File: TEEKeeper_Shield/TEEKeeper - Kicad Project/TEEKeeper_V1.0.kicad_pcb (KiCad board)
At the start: 2 copper layers, 99.4 x 94.5 mm, 29 parts

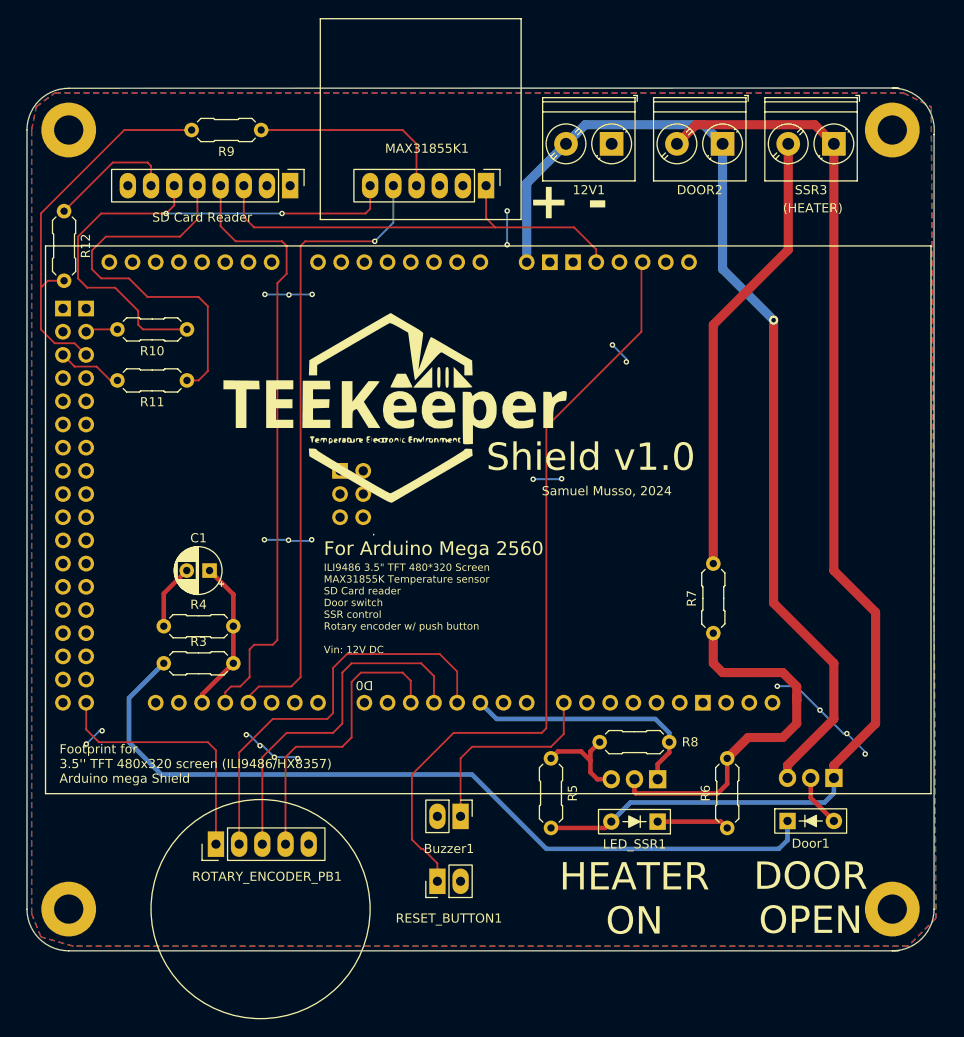
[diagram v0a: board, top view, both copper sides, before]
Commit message: Resolved minor issues
Fixed broken / bad designed reference connections, fixed pcb courtyard and edges, general cleanup
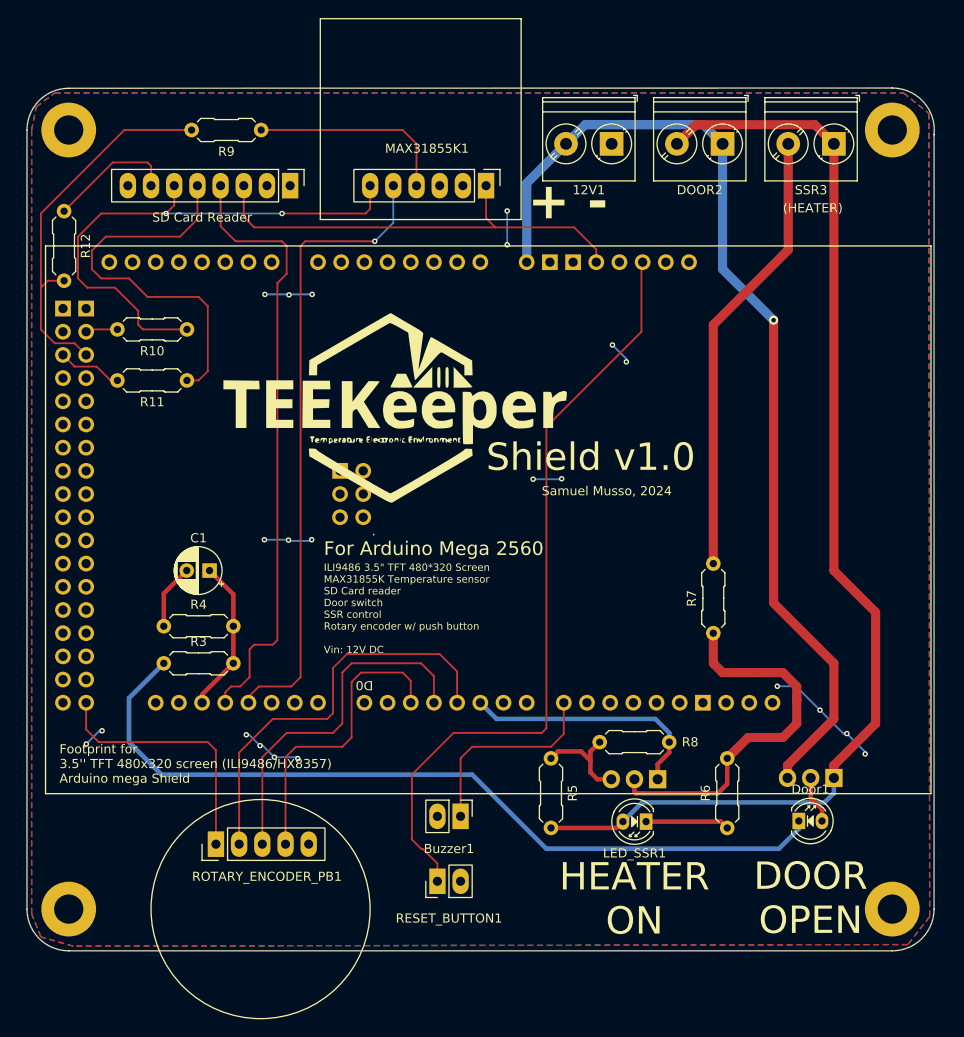
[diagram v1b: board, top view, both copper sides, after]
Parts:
- Door1, LED_SSR1: footprint PCM_LED_THT_AKL:LED_Indicator_D1.8mm_W2.44mm_L7.62mm -> PCM_LED_THT_AKL:LED_D4.0mm
- moved LED_SSR1 1.27 mm to (192.3, 106.2)
- moved Door1 1.24 mm to (209.0, 106.2)
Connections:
- A1 pad 5V1: /System_Shield/Digital_PCB/5V -> 5V
- A1 pad 5V3: /System_Shield/Digital_PCB/5V -> 5V
- A1 pad 5V4: /System_Shield/Digital_PCB/5V -> unconnected-(A1-5V-Pad5V4)
- MAX31855K1 pad 1: /System_Shield/Digital_PCB/5V -> 5V
- ROTARY_ENCODER_PB1 pad 1: /System_Shield/Digital_PCB/5V -> 5V
- SD_CARD1 pad 3: /System_Shield/Digital_PCB/5V -> 5V
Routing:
- net 5V: track 0.00 -> 78.3 mm
- net /System_Shield/Digital_PCB/5V: track 78.3 -> 0.00 mm
- net Net-(LED_SSR1-Pad1): track 7.91 -> 9.17 mm
- net Net-(P_DOOR1-D): track 5.77 -> 5.23 mm
- net Net-(Door1-Pad1): track 89.7 -> 90.2 mm
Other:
- outline, holes or cut-outs redrawn

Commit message: Minor changes
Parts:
- moved ROTARY_ENCODER_PB1 3.43 mm to (141.7, 108.7)
- moved R6 2.54 mm to (198.6, 106.9)
- moved R8 2.54 mm to (184.7, 97.5)
- moved RESET_BUTTON1 2.54 mm to (166.9, 112.8)
- moved Buzzer1 2.54 mm to (169.4, 105.7)
- moved Door1 2.54 mm to (206.5, 106.2)
- moved LED_SSR1 2.54 mm to (189.7, 106.2)
- moved N_SSR1 2.54 mm to (191.0, 101.6)
- moved P_DOOR1 2.54 mm to (210.3, 101.5)
- moved R5 2.54 mm to (179.3, 99.3)
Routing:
- net GND: track 60.2 -> 84.0 mm, vias 22 -> 30
- net 5V: track 78.3 -> 74.8 mm
- net /System_Shield/Digital_PCB/D4: track 45.5 -> 48.7 mm
- net /System_Shield/Digital_PCB/D2_INTRR: track 33.4 -> 36.6 mm
- net /System_Shield/Digital_PCB/D3_INTRR: track 39.4 -> 42.6 mm
- net /System_Shield/Analog_PCB/HEATER_CT: track 27.7 -> 25.1 mm
- net Net-(N_SSR1-D): track 42.1 -> 44.1 mm
- net Net-(P_DOOR1-G): track 126.4 -> 124.9 mm
- net Net-(Door1-Pad1): track 90.2 -> 88.7 mm
- net /System_Shield/Digital_PCB/RESET: track 85.2 -> 84.3 mm
- net /System_Shield/Digital_PCB/BUZ: track 22.2 -> 22.7 mm

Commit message: Added connector cutouts
Added cutouts for the Arduino Mega barrel and USB-A connector. 
Rerouted connections accordingly.
Added more vias to GND plane along SPI lines and other parallel strips. 
Added clearance for some components.
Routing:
- net /System_Shield/Digital_PCB/D4: track 48.7 -> 52.8 mm
- net GND: track 84.0 -> 86.3 mm, vias 30 -> 123
- net Net-(P_DOOR1-G): track 124.9 -> 127.0 mm
- net /System_Shield/Digital_PCB/D3_INTRR: track 42.6 -> 44.5 mm
- net Net-(Door1-Pad1): track 88.7 -> 87.7 mm
- net Net-(N_SSR1-D): track 44.1 -> 43.6 mm
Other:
- outline, holes or cut-outs redrawn

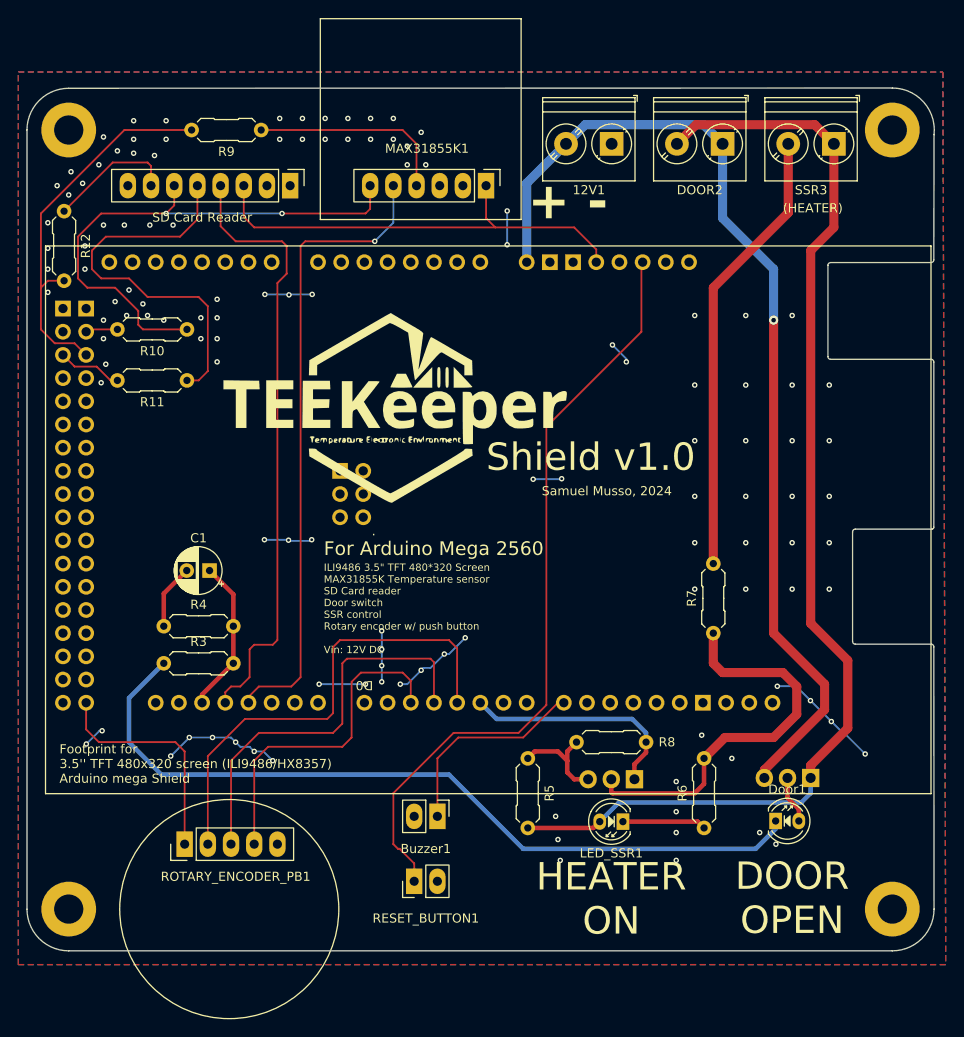
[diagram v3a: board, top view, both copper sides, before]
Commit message: Reworked Arduino Mega clearance
Due to some clones having their USB and barrel connector placed in slightly different locations, added a big cutout and rerouted tracks accordingly

uniformed 12V copper lines width
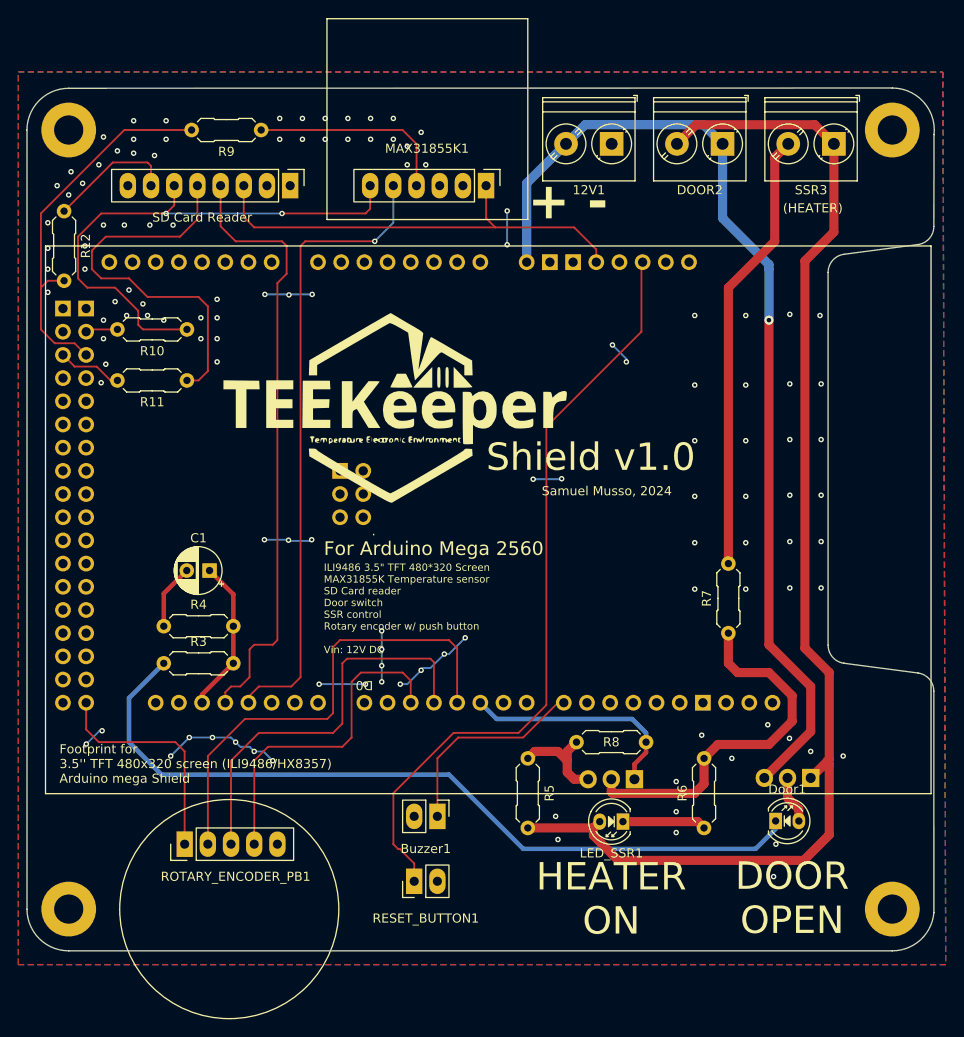
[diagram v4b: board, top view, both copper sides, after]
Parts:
- moved R7 1.65 mm to (201.3, 85.6)
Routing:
- net GND: track 86.3 -> 73.6 mm, vias 123 -> 122
- net Net-(P_DOOR1-G): track 127.0 -> 136.9 mm
- net Net-(N_SSR1-D): track 43.6 -> 40.7 mm
- net /System_Shield/Analog_PCB/VIN: track 110.5 -> 109.2 mm
- net Net-(R7-Pad2): track 49.4 -> 48.7 mm
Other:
- outline, holes or cut-outs redrawn
